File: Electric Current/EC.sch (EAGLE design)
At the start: 21 parts, among them IC1 LD117AS33TR, IC3 LTC-1966MSOP-8

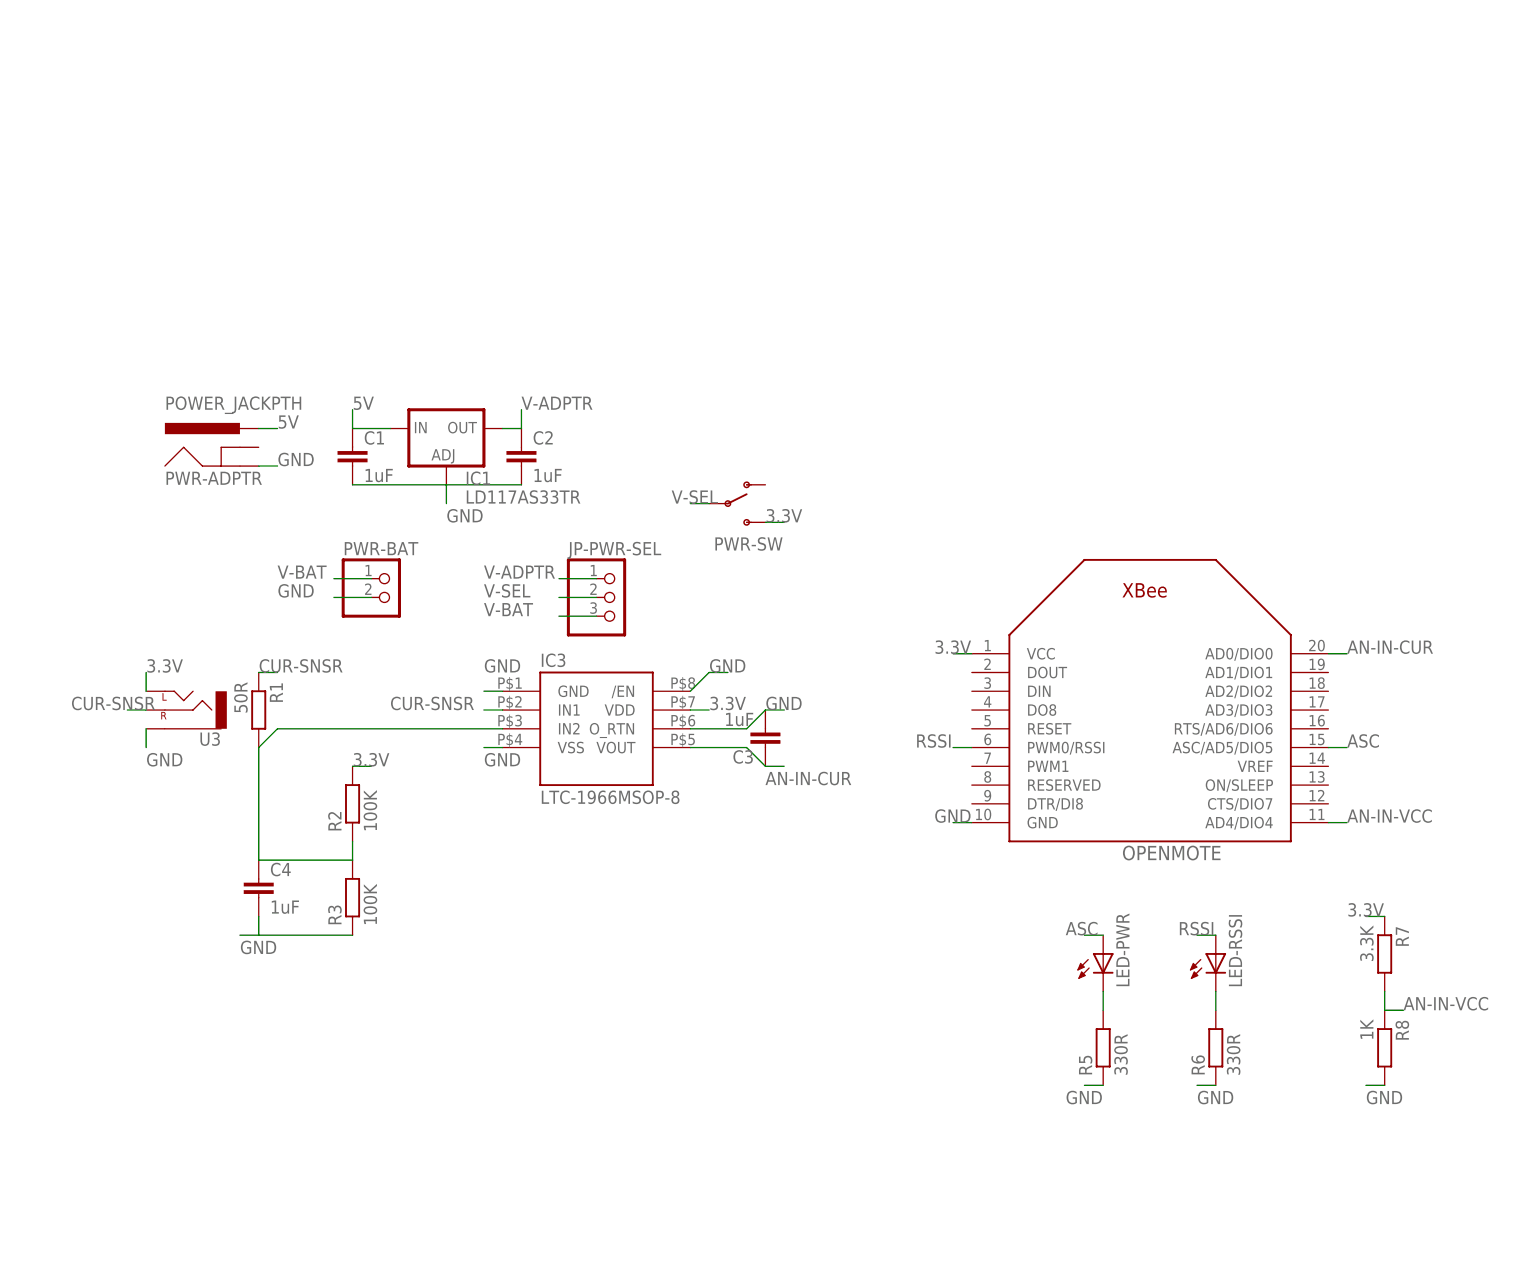
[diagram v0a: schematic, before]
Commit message: 3 phase meter, add spacer, reset LTC 1966 dim
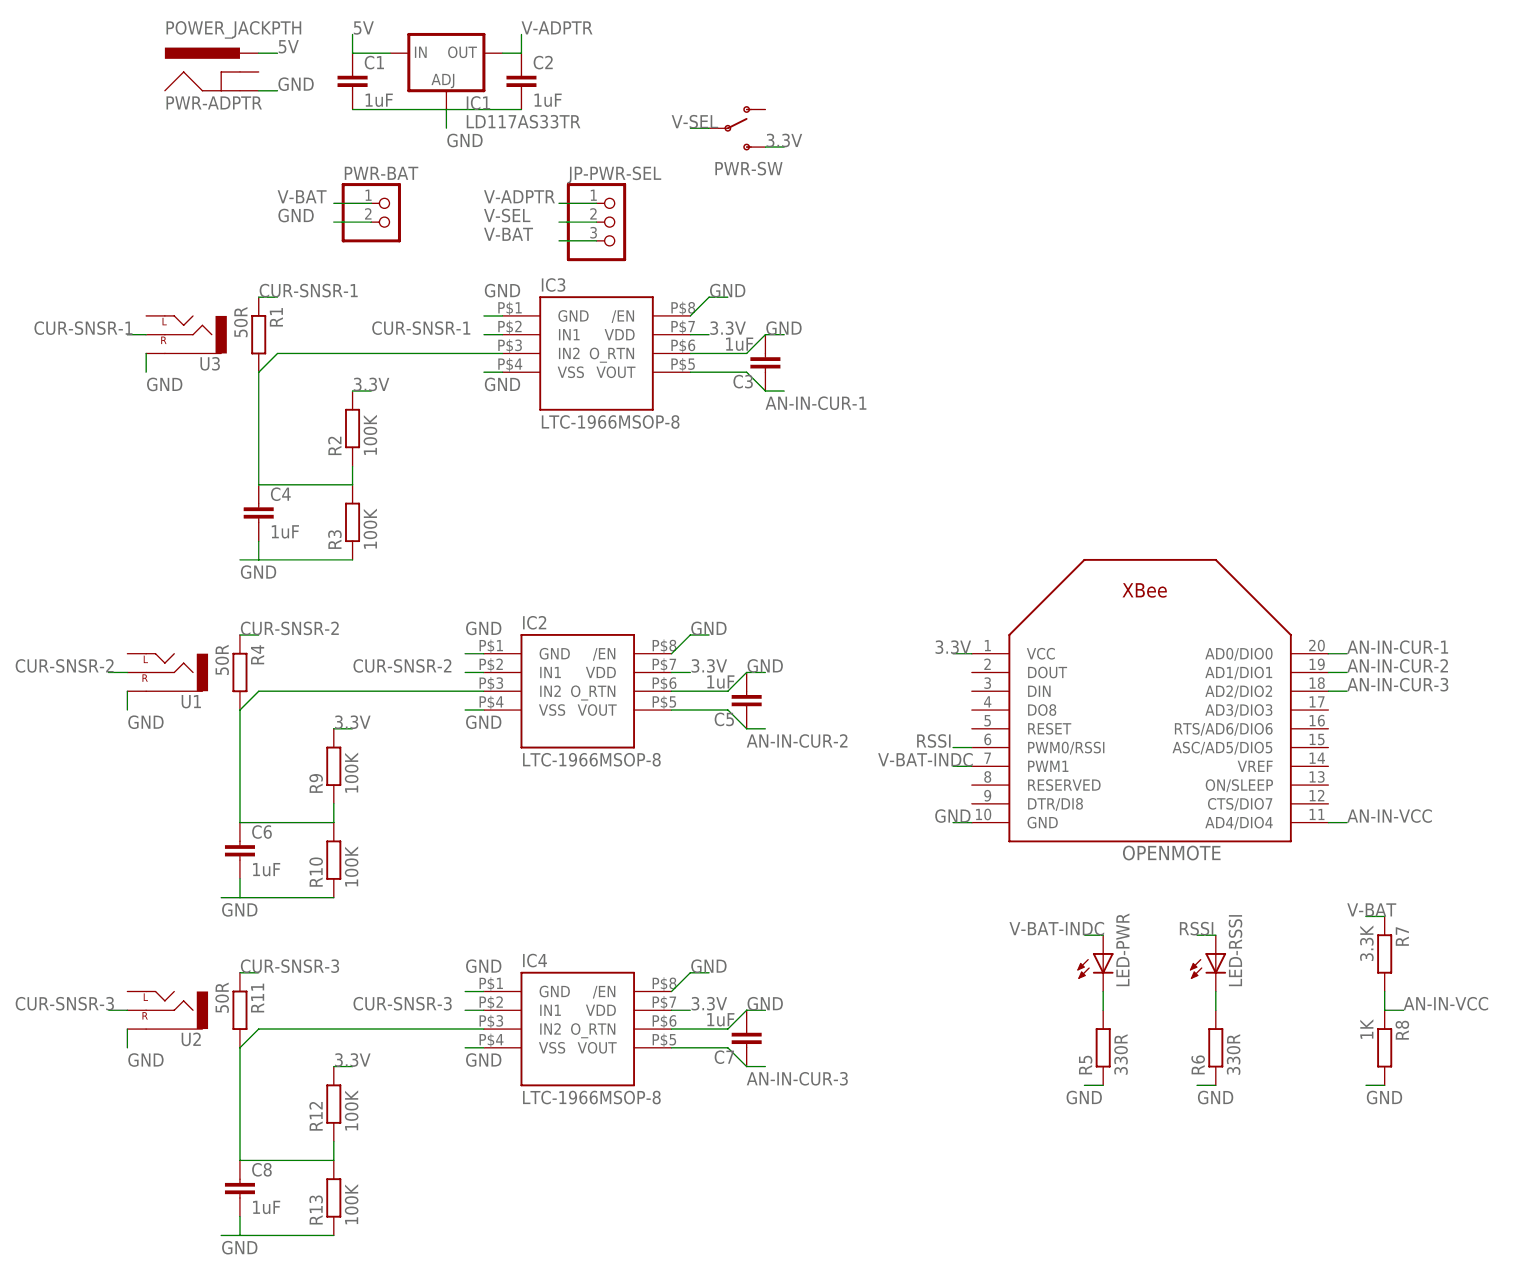
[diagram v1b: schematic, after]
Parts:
- added C5, C6, C7, C8: 1uF, resistor:C-EUC0805
- added IC2, IC4: LTC-1966MSOP-8, custom-tigor:LTC-1966MSOP-8
- added R10, R12, R13, R9: 100K, resistor:R-EU_R0603
- added R11, R4: 50R, resistor:R-EU_R0603
- added U1, U2: (no value), SparkFun-Connectors:AUDIO-JACKSMD2
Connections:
- net AN-IN-CUR renamed AN-IN-CUR-1
- net CUR-SNSR renamed CUR-SNSR-1
- removed net ASC: LED-PWR.A, OPENMOTE.ASC/AD5/DIO5
- new net AN-IN-CUR-2: C5.1, IC2.VOUT, OPENMOTE.AD1/DIO1
- new net AN-IN-CUR-3: C7.1, IC4.VOUT, OPENMOTE.AD2/DIO2
- new net CUR-SNSR-2: IC2.IN1, R4.1, U1.RIGHT
- new net CUR-SNSR-3: IC4.IN1, R11.1, U2.RIGHT
- new net N$4: C6.1, IC2.IN2, R10.2, R4.2, R9.1
- new net N$5: C8.1, IC4.IN2, R11.2, R12.1, R13.2
- new net V-BAT-INDC: LED-PWR.A, OPENMOTE.PWM1
- net 3.3V: now also IC2.VDD, IC4.VDD, R12.2, R9.2; no longer R7.1, U3.LEFT
- net GND: now also C5.2, C6.2, C7.2, C8.2, IC2./EN, IC2.GND, IC2.O_RTN, IC2.VSS, IC4./EN, IC4.GND, IC4.O_RTN, IC4.VSS, R10.1, R13.1, U1.SLEEVE, U2.SLEEVE
- net V-BAT: now also R7.1
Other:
- moved on the sheet: C1, C2, C3, C4, IC1, IC3, JP-PWR-SEL, PWR-ADPTR, PWR-BAT, PWR-SW, R1, R2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
